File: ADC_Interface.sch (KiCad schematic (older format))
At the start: 21 parts, among them J2 ADC_SPI_CONN, U3 ADS131M04, Y3 8.192 MHz

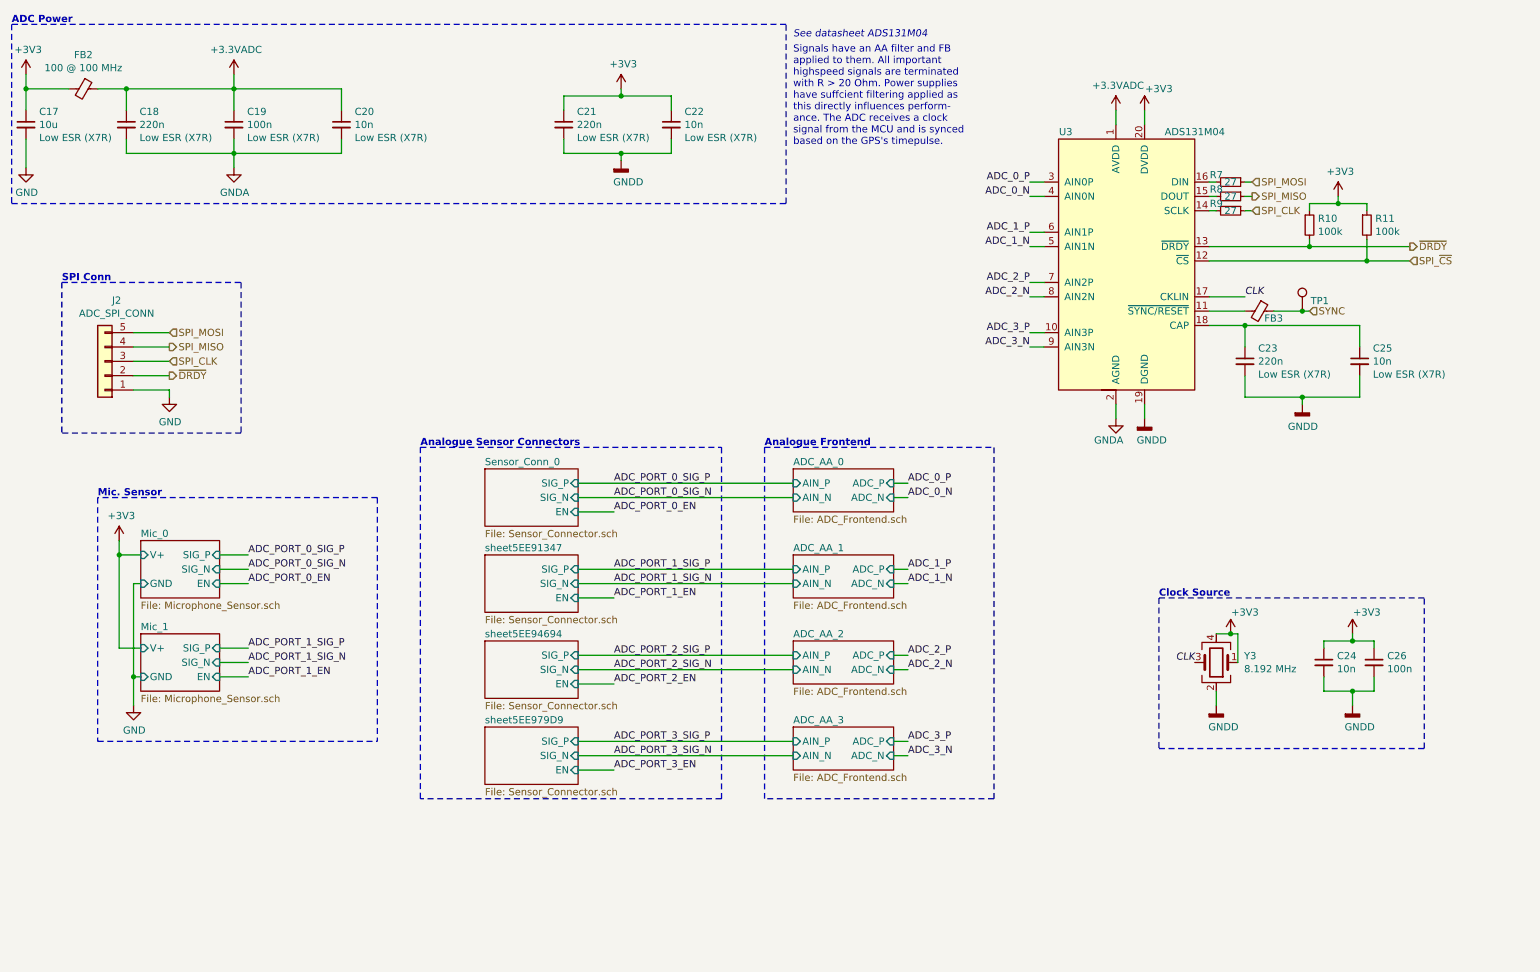
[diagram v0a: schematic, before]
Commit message: Assign footprints for all components
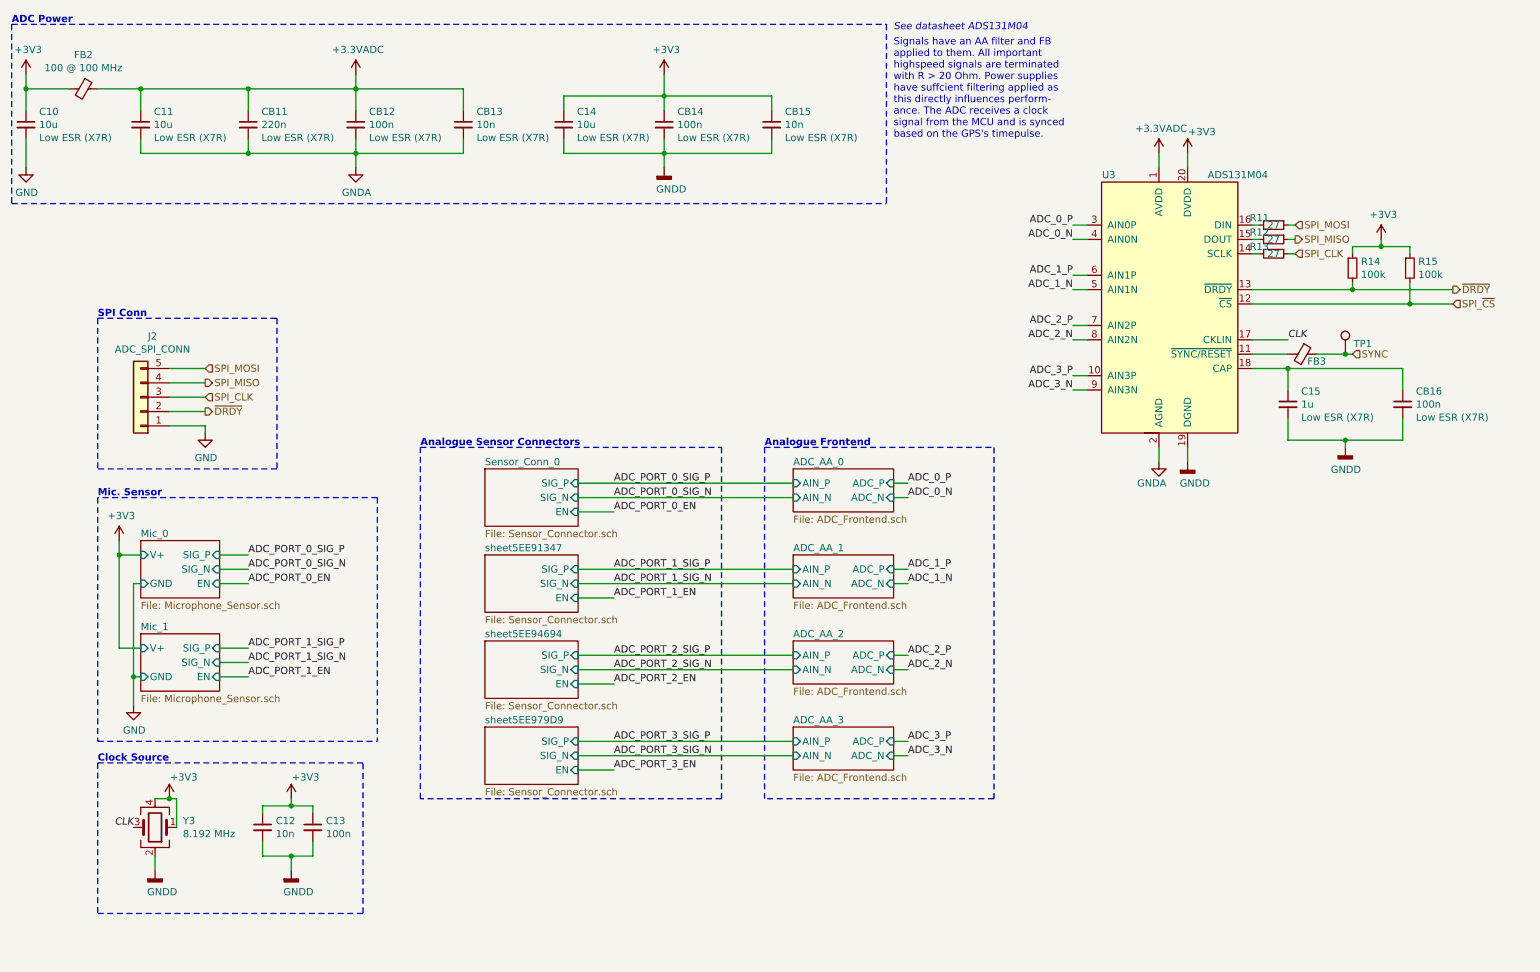
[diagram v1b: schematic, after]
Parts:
- added C11, C14: 10u, Capacitor_SMD:C_0805_2012Metric_Pad1.15x1.40mm_HandSolder, symbol Device:C_Small
- C10: renamed from C17; footprint (none) -> Capacitor_SMD:C_0805_2012Metric_Pad1.15x1.40mm_HandSolder; MFN (none) -> C0805C106K9PACTU; Mfr. (none) -> KEMET
- C12: renamed from C24; footprint (none) -> Capacitor_SMD:C_0603_1608Metric_Pad1.05x0.95mm_HandSolder
- C13: renamed from C26; footprint (none) -> Capacitor_SMD:C_0603_1608Metric_Pad1.05x0.95mm_HandSolder
- C15: renamed from C23; value 220n -> 1u; footprint (none) -> Capacitor_SMD:C_0603_1608Metric_Pad1.05x0.95mm_HandSolder
- CB11: renamed from C18; footprint (none) -> Capacitor_SMD:C_0603_1608Metric_Pad1.05x0.95mm_HandSolder
- CB12: renamed from C19; footprint (none) -> Capacitor_SMD:C_0603_1608Metric_Pad1.05x0.95mm_HandSolder
- CB13: renamed from C20; footprint (none) -> Capacitor_SMD:C_0603_1608Metric_Pad1.05x0.95mm_HandSolder
- CB14: renamed from C21; value 220n -> 100n; footprint (none) -> Capacitor_SMD:C_0603_1608Metric_Pad1.05x0.95mm_HandSolder
- CB15: renamed from C22; footprint (none) -> Capacitor_SMD:C_0603_1608Metric_Pad1.05x0.95mm_HandSolder
- CB16: renamed from C25; value 10n -> 100n; footprint (none) -> Capacitor_SMD:C_0603_1608Metric_Pad1.05x0.95mm_HandSolder
- FB2: value Ferrite_Bead_Small -> BLM18KG101TZ1D; footprint (none) -> Inductor_SMD:L_0603_1608Metric_Pad1.05x0.95mm_HandSolder; MPN (none) -> BLM18EG101TZ1D; Mfr. (none) -> Murata Semiconductor
- FB3: footprint (none) -> Inductor_SMD:L_0402_1005Metric; MPN (none) -> BLM15HD102SN1D; Mfr. (none) -> Murata Semiconductor
- J2: footprint (none) -> Connector_PinHeader_1.27mm:PinHeader_1x05_P1.27mm_Vertical
- R11: renamed from R7; footprint (none) -> Resistor_SMD:R_0603_1608Metric_Pad1.05x0.95mm_HandSolder
- R12: renamed from R8; footprint (none) -> Resistor_SMD:R_0603_1608Metric_Pad1.05x0.95mm_HandSolder
- R13: renamed from R9; footprint (none) -> Resistor_SMD:R_0603_1608Metric_Pad1.05x0.95mm_HandSolder; MPN (none) -> RC0603FR-0727RL; Mfr. (none) -> Yageo
- R14: renamed from R10; footprint (none) -> Resistor_SMD:R_0603_1608Metric_Pad1.05x0.95mm_HandSolder; MPN (none) -> RC0603FR-07100KL; Mfr. (none) -> Yageo
- R15: renamed from R11; footprint (none) -> Resistor_SMD:R_0603_1608Metric_Pad1.05x0.95mm_HandSolder; MPN (none) -> RC0603FR-07100KL; Mfr. (none) -> Yageo
- TP1: footprint (none) -> TestPoint:TestPoint_Pad_D1.0mm
- U3: footprint (none) -> Package_SO:TSSOP-20_4.4x6.5mm_P0.65mm
- Y3: footprint (none) -> grootvoet:CDFN-4_3.2x2.5mm
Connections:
- net +3.3VADC: now also C11.1
- net +3V3: now also C14.1
- net GNDA: now also C11.2
- net GNDD: now also C14.2
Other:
- moved on the sheet: C12, C13, C15, CB11, CB12, CB13, CB14, CB15, CB16, FB3, J2, R11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

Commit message: Change Mic Preamp
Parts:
- removed CB11: 220n, Capacitor_SMD:C_0603_1608Metric_Pad1.05x0.95mm_HandSolder, symbol Device:C_Small
- C10, C11: MFN C0805C106K9PACTU -> (none); MPN (none) -> C0805C106K9PACTU
- C12: renamed from C14; MFN C0805C106K9PACTU -> (none); MPN (none) -> C0805C106K9PACTU
- C13: renamed from C15; MPN (none) -> C0603C105K8RACTU; Mfr. (none) -> KEMET
- CB11: renamed from C12; MPN (none) -> C0603C103J5RACTU; Mfr. (none) -> KEMET
- CB12: MPN (none) -> C0603C104M5RACTU; Mfr. (none) -> KEMET
- CB13: renamed from C13; MPN (none) -> C0603C104M5RACTU; Mfr. (none) -> KEMET
- CB14: renamed from CB13; MPN (none) -> C0603C103J5RACTU; Mfr. (none) -> KEMET
- CB15: renamed from CB14; MPN (none) -> C0603C104M5RACTU; Mfr. (none) -> KEMET
- CB16: renamed from CB15; MPN (none) -> C0603C103J5RACTU; Mfr. (none) -> KEMET
- CB17: renamed from CB16; MPN (none) -> C0603C104M5RACTU; Mfr. (none) -> KEMET
- FB2, FB3: Mfr. Murata Semiconductor -> Murata Electronics
- R11, R12: MPN (none) -> RC0603FR-0727RL; Mfr. (none) -> Yageo
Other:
- moved on the sheet: CB12, CB14

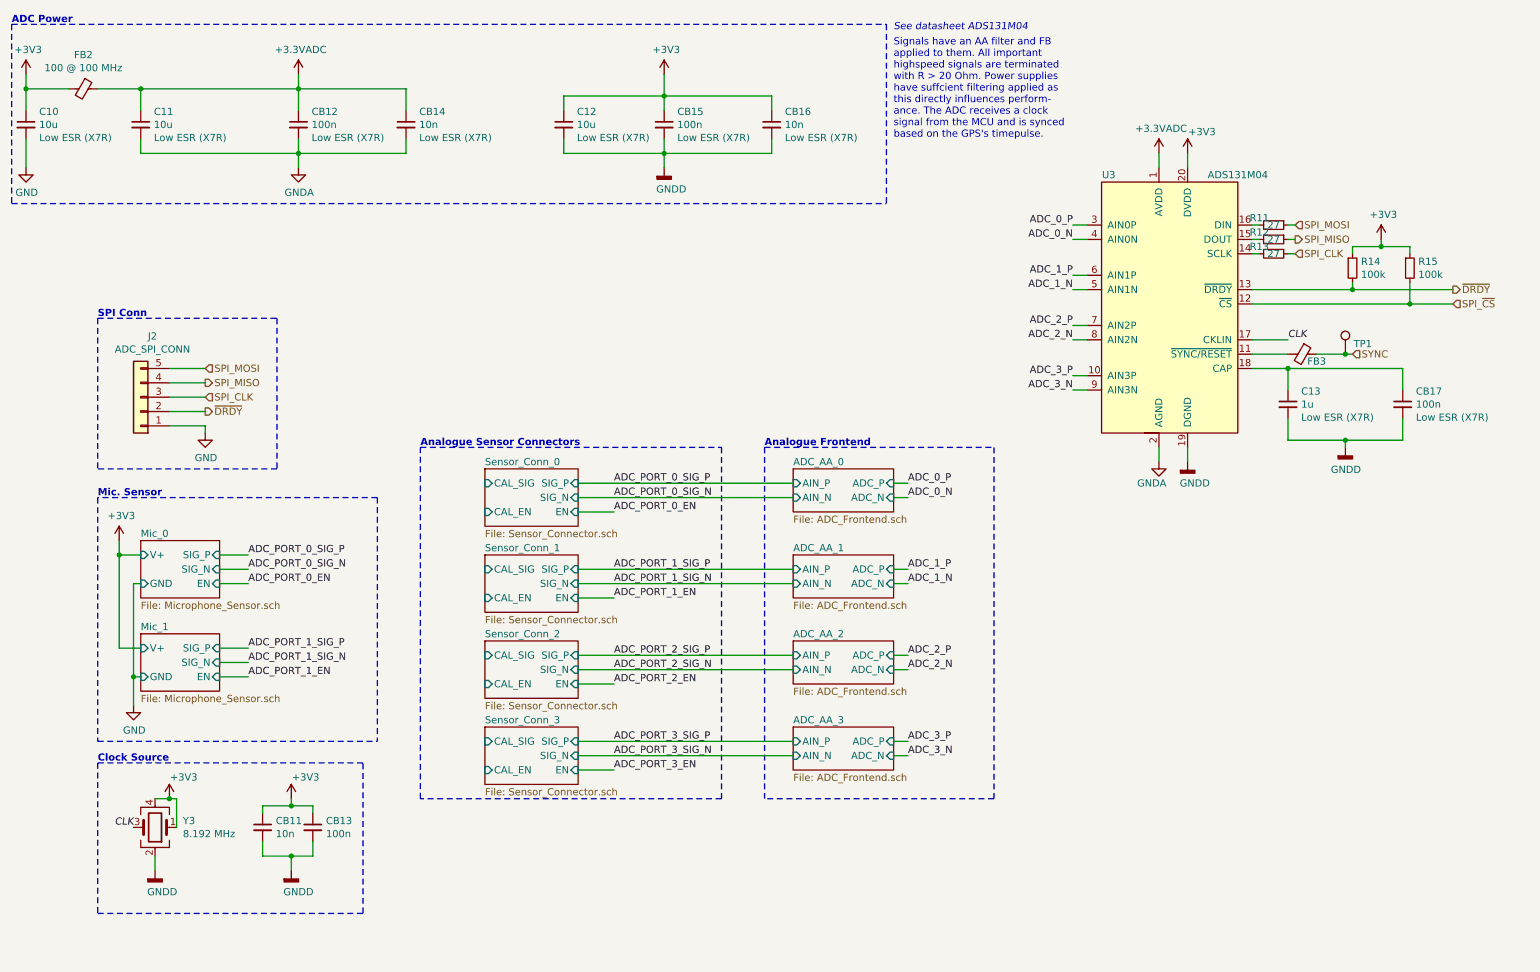
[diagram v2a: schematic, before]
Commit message: Fix BOM ref
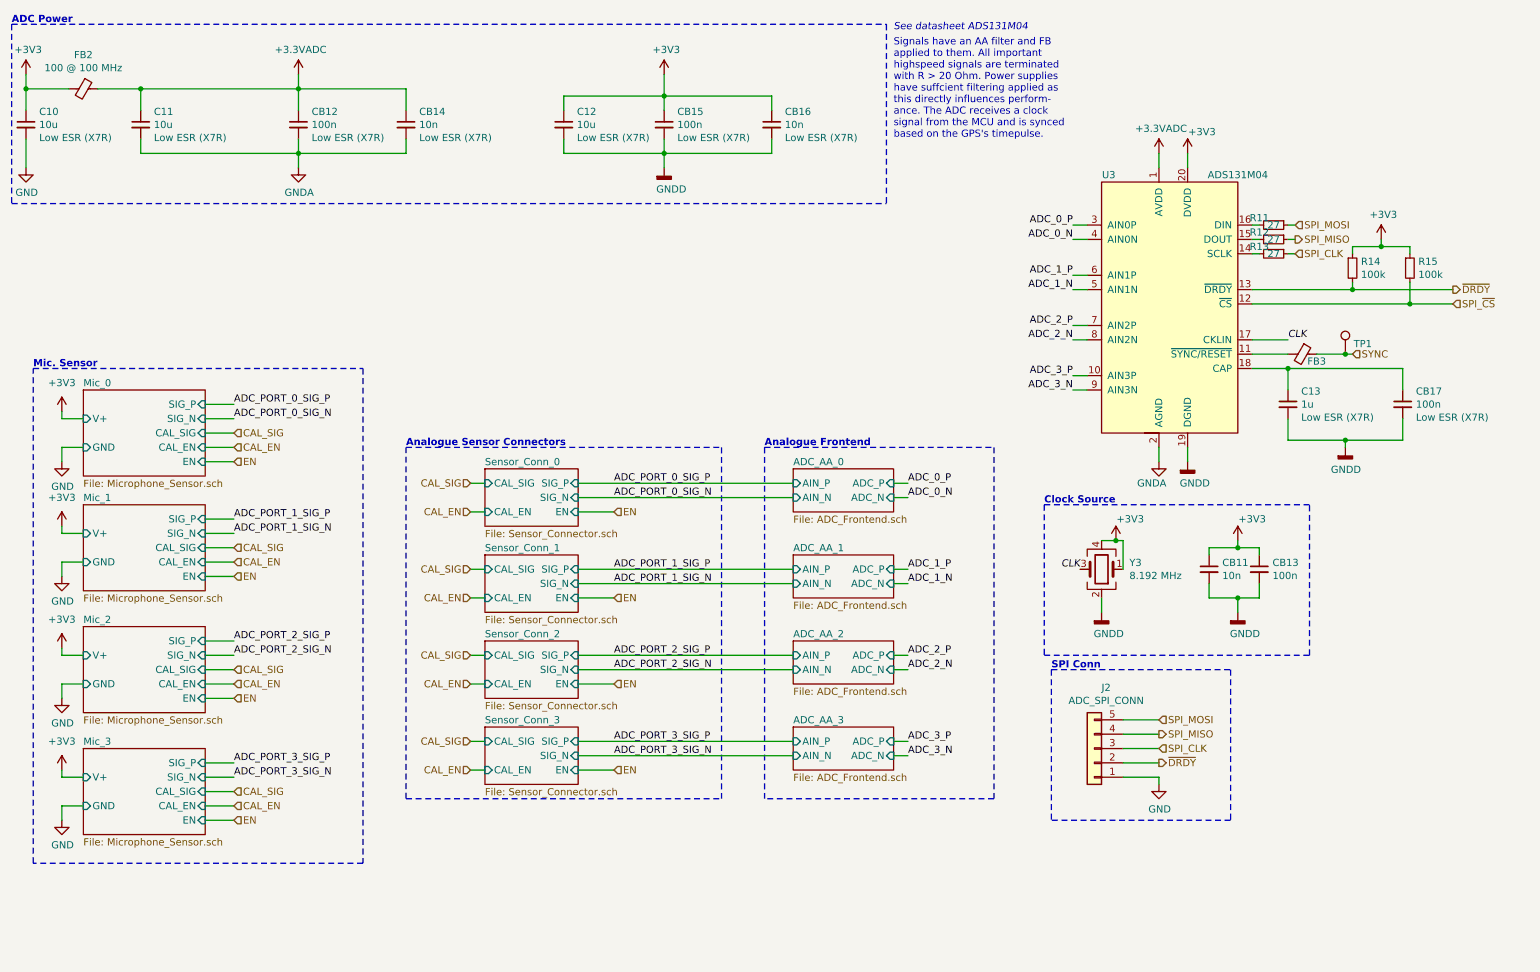
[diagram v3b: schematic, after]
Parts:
- FB2: MPN BLM18EG101TZ1D -> BLM18KG101TZ1D
- U3: MPN (none) -> ADS131M04IPWR; Mfr. (none) -> Texas Instruments
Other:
- moved on the sheet: CB11, CB13, J2, Y3

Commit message: PCB Layout Checkpoint
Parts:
- removed C10: 10u, Capacitor_SMD:C_0805_2012Metric_Pad1.15x1.40mm_HandSolder, symbol Device:C_Small
- removed C13: 1u, Capacitor_SMD:C_0603_1608Metric_Pad1.05x0.95mm_HandSolder, symbol Device:C_Small
- removed R11, R12, R13: 27, Resistor_SMD:R_0603_1608Metric_Pad1.05x0.95mm_HandSolder, symbol Device:R_Small
- added R92: 27, Resistor_SMD:R_0603_1608Metric_Pad1.05x0.95mm_HandSolder, symbol Device:R_Small
- CB17: value 100n -> 220n; MPN C0603C104M5RACTU -> (none); Mfr. KEMET -> (none)
- renumbered CB12 to CB11, CB14 to CB12, CB15 to CB13, CB16 to CB14, CB11 to CB15, CB13 to CB16
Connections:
- net CLK: now also R92.1; no longer U3.17 (CKLIN)
- net SPI_CLK: now also U3.14 (SCLK)
- net SPI_MISO: now also U3.15 (DOUT)
- net SPI_MOSI: now also U3.16 (DIN)
- new net: R92.2, U3.17 (CKLIN)
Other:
- moved on the sheet: CB17, TP1

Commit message: Major Commit with Final PCB Design
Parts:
- removed J2: ADC_SPI_CONN, Connector_PinHeader_1.27mm:PinHeader_1x05_P1.27mm_Vertical, symbol Connector_Generic:Conn_01x05
- removed TP1: TestPoint, TestPoint:TestPoint_Pad_D1.0mm, symbol Connector:TestPoint
- added R11, R12, R13: 100k, Resistor_SMD:R_0603_1608Metric_Pad1.05x0.95mm_HandSolder, symbol Device:R_Small
- CB17: MPN (none) -> C0603C224K8RACTU; Mfr. (none) -> KEMET
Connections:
- net +3V3: now also R11.1
- net CAL_EN: now also R12.1
- net CAL_SIG: now also R13.1
- net EN: now also R11.2
- net GND: now also R12.2, R13.2
- net ADC_CLK: now reaches R92.2, U3.17 (CKLIN)
- net CLK: no longer names the net of R92.1, Y3.3
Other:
- note removed: "SPI Conn"
- moved on the sheet: R92, Y3
